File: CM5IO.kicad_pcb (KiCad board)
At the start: 4 copper layers, 160 x 90 mm, 57 parts, among them J11 USB_C_Receptacle_USB2.0, J12 USB3_A, J14 JST_SHBM04B-SRSS-TB, J22 690-019-298-412, J3 Conn_01x03, J4 Bus_M.2_Socket_M, J7 Micro_SD_Card_Det, SW1 Right angle Tact button, U12 RT9742SNGV, U18 RT9742GGJ5, U5 74LVC1G07SE-7, U6 AP22653W6, U7 ASEK-32.768KHZ-L-R-T, U8 AP3441SHE-7B

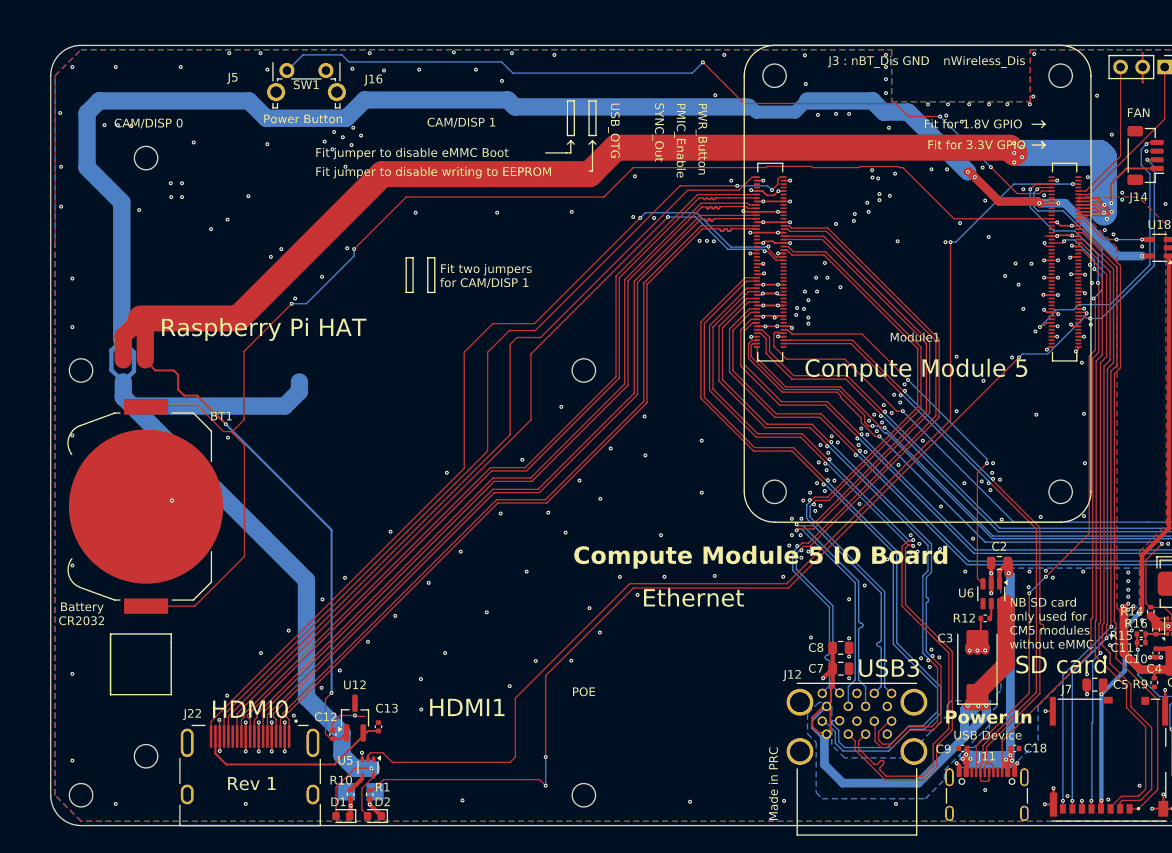
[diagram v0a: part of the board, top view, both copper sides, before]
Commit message: remove more components, set stackup to JLC04161H-7628
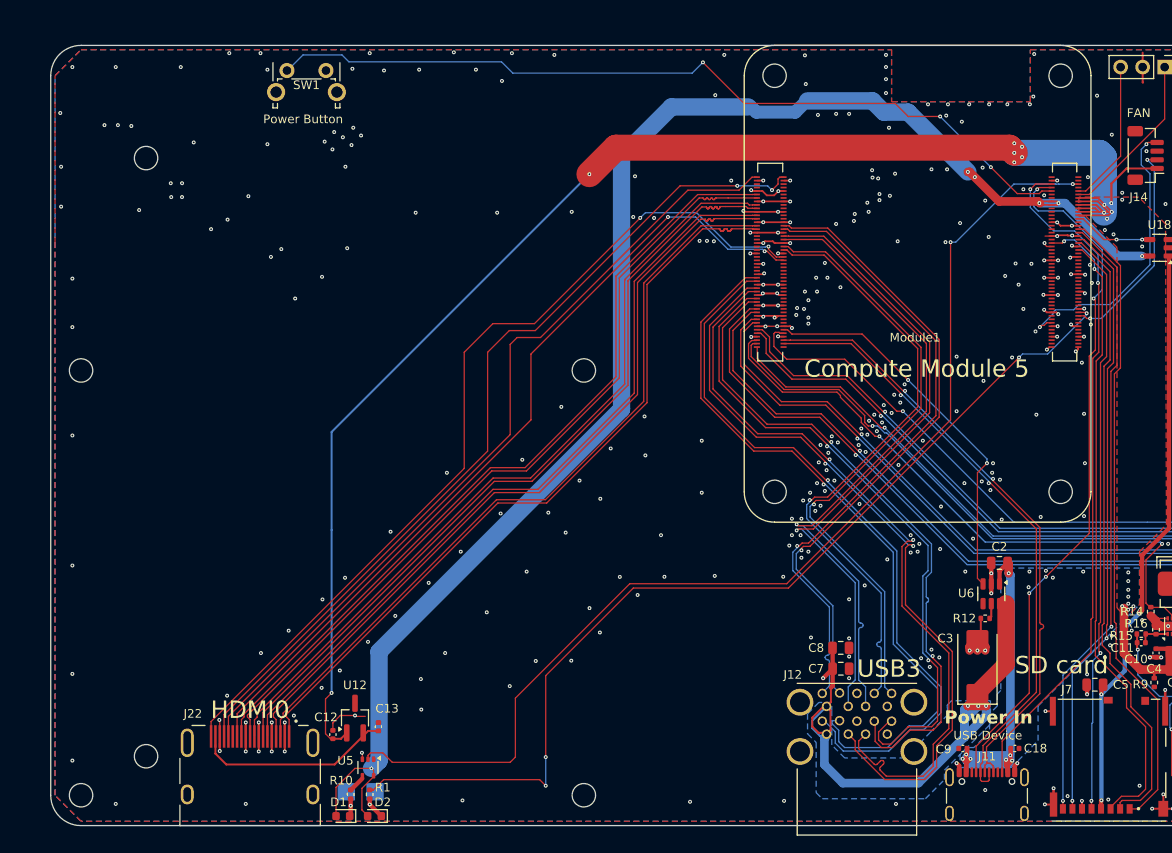
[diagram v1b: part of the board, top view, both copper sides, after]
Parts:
- removed BT1: Battery_Cell, CM5IO:BatteryHolder_Keystone_3034_1x20mm
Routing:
- net /CM5_GPIO ( Ethernet, GPIO, SDCARD)/VBAT: track 154.8 -> 0.00 mm, vias 2 -> 0
- net /+3.3v: track 271.0 -> 173.3 mm
- net /+5v: track 284.2 -> 237.7 mm
- net GND: track 711.4 -> 708.4 mm, vias 431 -> 429
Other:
- board text removed: "Battery CR2032"
- board text removed: "CAM/DISP 0"
- board text removed: "CAM/DISP 1"
- board text removed: "Compute Module 5 IO Board"
- board text removed: "Ethernet"
- board text removed: "Fit for 1.8V GPIO"
- board text removed: "Fit for 3.3V GPIO"
- board text removed: "Fit jumper to disable eMMC Boot"
- board text removed: "Fit jumper to disable writing to EEPROM"
- board text removed: "Fit two jumpers for CAM/DISP 1"
- board text removed: "HDMI1"
- board text removed: "J16"
- board text removed: "J3 : nBT_Dis GND"
- board text removed: "J5"
- board text removed: "Made in PRC"
- board text removed: "NB SD card only used for CM5 modules without eMMC"
- board text removed: "PMIC_Enable"
- board text removed: "POE"
- board text removed: "PWR_Button"
- board text removed: "Raspberry Pi HAT"
- board text removed: "Rev 1"
- board text removed: "SYNC_Out"
- board text removed: "USB_OTG"
- board text removed: "nWireless_Dis"
